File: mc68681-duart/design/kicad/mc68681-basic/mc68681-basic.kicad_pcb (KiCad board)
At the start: 4 copper layers, 80 x 110 mm, 35 parts, among them IC1 68681, IC2 74HCT245, IC3 74HCT245, IC4 74HCT245, IC5 74125, IC6 IC6_DECO.PLD, IC7 IC7_UART_.PLD, J1 Conn_02x32_Odd_Even, J2 EXTBUS, J3 UART_A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

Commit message: Initial work on schematic, board ripped up
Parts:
- removed JP1, JP2, JP3, JP4: Jumper, Connector_PinHeader_2.54mm:PinHeader_1x02_P2.54mm_Vertical
- added JP1-5: Conn_02x05_Odd_Even, Connector_PinHeader_2.54mm:PinHeader_2x05_P2.54mm_Vertical, F.Cu at (62.8, 136.7)
- IC1: value 68681 -> XR68C681CJTR-F; footprint Package_DIP:DIP-40_W15.24mm_Socket_LongPads -> Package_LCC:PLCC-44_THT-Socket
- moved C12 47.4 mm to (94.5, 75.4)
- moved C10 47.0 mm to (84.7, 75.4)
- moved C6 46.8 mm to (74.9, 75.3)
- moved C5 30.8 mm to (95.2, 114.3)
- moved C3 23.5 mm to (74.2, 114.3)
- moved Q1 22.4 mm to (82.3, 114.3), turned to 0 degrees
- moved IC1 22.1 mm to (86.0, 87.2)
- moved R2 14.1 mm to (79.6, 122.1), turned to 0 degrees
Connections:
- IC1 pad 1: A1 -> Net-(IC1-Pad1)
- IC1 pad 10: RXDB -> UDTACK
- IC1 pad 11: TXDB -> RXDB
- IC1 pad 12: CTSB -> Net-(IC1-Pad12)
- IC1 pad 13: OP3 -> TXDB
- IC1 pad 14: OP5 -> CTSB
- IC1 pad 15: OP7 -> OP3
- IC1 pad 16: BD1 -> OP5
- IC1 pad 17: BD3 -> OP7
- IC1 pad 18: BD5 -> BD1
- IC1 pad 19: BD7 -> BD3
- IC1 pad 2: IP3 -> A1
- IC1 pad 20: GND -> BD5
- IC1 pad 21: IRQ -> BD7
- IC1 pad 22: BD6 -> GND
- IC1 pad 23: BD4 -> Net-(IC1-Pad23)
- IC1 pad 24: BD2 -> IRQ
- IC1 pad 25: BD0 -> BD6
- IC1 pad 26: OP6 -> BD4
- IC1 pad 27: OP4 -> BD2
- IC1 pad 28: OP2 -> BD0
- IC1 pad 29: CTSA -> OP6
- IC1 pad 3: A2 -> IP3
- IC1 pad 30: TXDA -> OP4
- IC1 pad 31: RXDA -> OP2
- IC1 pad 32: Net-(C3-Pad1) -> CTSA
- IC1 pad 33: Net-(C5-Pad1) -> TXDA
- IC1 pad 34: RESET -> Net-(IC1-Pad34)
- IC1 pad 35: SEL -> RXDA
- IC1 pad 36: IP2 -> Net-(C3-Pad1)
- IC1 pad 37: Net-(IC1-Pad37) -> Net-(C5-Pad1)
- IC1 pad 38: IP5 -> RESET
- IC1 pad 39: IP4 -> SEL
- IC1 pad 4: IP1 -> A2
- IC1 pad 40: VCC -> IP2
- IC1 pad 5: A3 -> IP1
- IC1 pad 6: A4 -> A3
- IC1 pad 7: IP0 -> A4
- IC1 pad 8: RnW -> IP0
- IC1 pad 9: UDTACK -> RnW
- IC7 pad 14: VPA -> UVPA
- IC7 pad 15: Net-(IC7-Pad15) -> IACK
- IC7 pad 7: Net-(IC7-Pad7) -> A1
- IC7 pad 8: Net-(IC7-Pad8) -> A2
- IC7 pad 9: Net-(IC7-Pad9) -> A3
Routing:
- net IRQ: track 116.1 -> 44.0 mm, vias 1 -> 0
- net IP0: track 73.7 -> 9.14 mm, vias 1 -> 0
- net UDTACK: track 52.0 -> 0.00 mm
- net A3: track 109.1 -> 59.6 mm, vias 2 -> 1
- net IP1: track 81.8 -> 33.1 mm, vias 1 -> 0
- net A4: track 104.4 -> 55.9 mm, vias 2 -> 1
- net BD7: track 46.6 -> 4.86 mm, vias 2 -> 0
- net RnW: track 82.5 -> 41.1 mm, vias 3 -> 1
- net CTSA: track 40.0 -> 0.00 mm, vias 2 -> 0
- net BD1: track 38.9 -> 6.37 mm, vias 1 -> 0
- net BD6: track 38.3 -> 5.91 mm, vias 1 -> 0
- net BD3: track 32.9 -> 2.78 mm
- net IP3: track 88.5 -> 58.9 mm
- net A1: track 67.1 -> 38.6 mm, vias 2 -> 1
- net RXDA: track 190.3 -> 162.7 mm
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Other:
- board text added: "Copyright ©2021 Ross Bamford & Contributors"
- board text added: "Revision 2 - March 2021"
- board text added: "r1 Mainboard"
- board text added: "r1.2 Mainboard"
- board text removed: "Copyright ©2020 Ross Bamford & Contributors"
- board text removed: "DTACK Enable"
- board text removed: "MC68681"
- board text removed: "Revision 1.1 - August 2020"

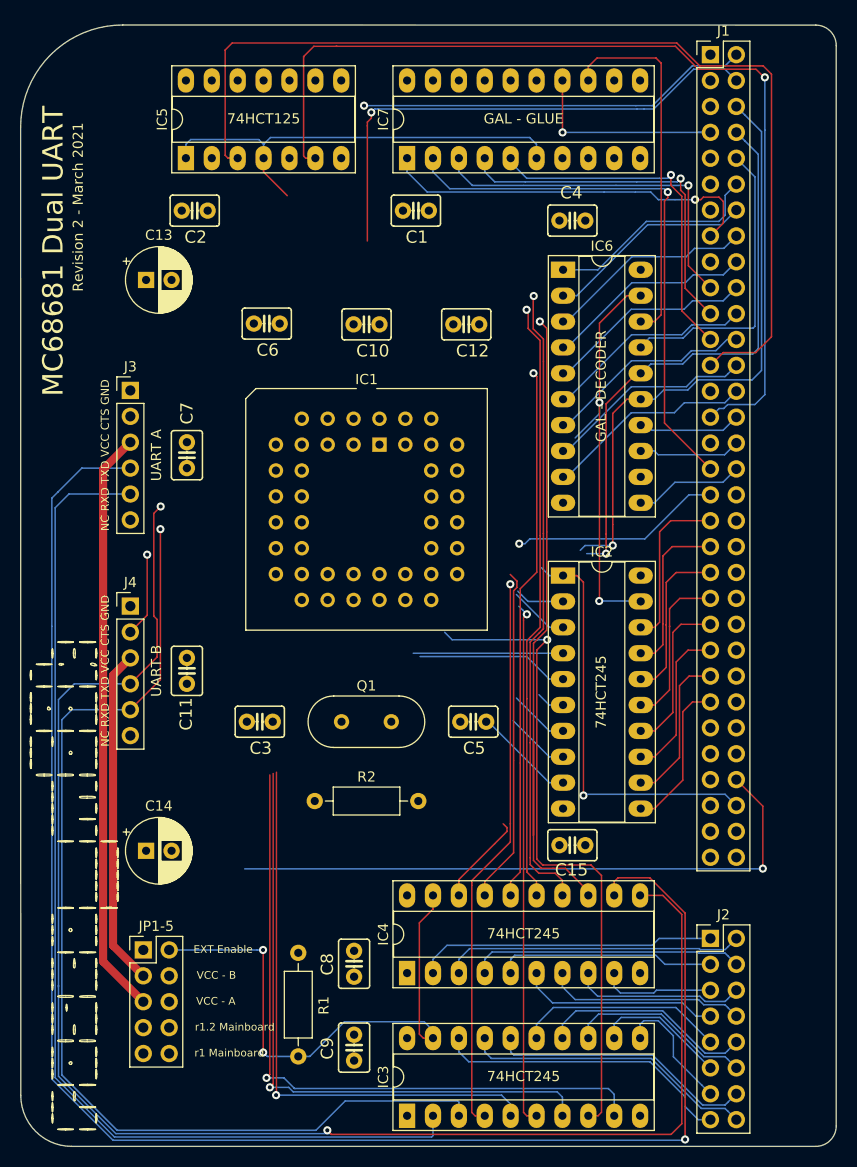
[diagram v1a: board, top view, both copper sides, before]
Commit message: First cut redo 68681 layout, add lib and pretty
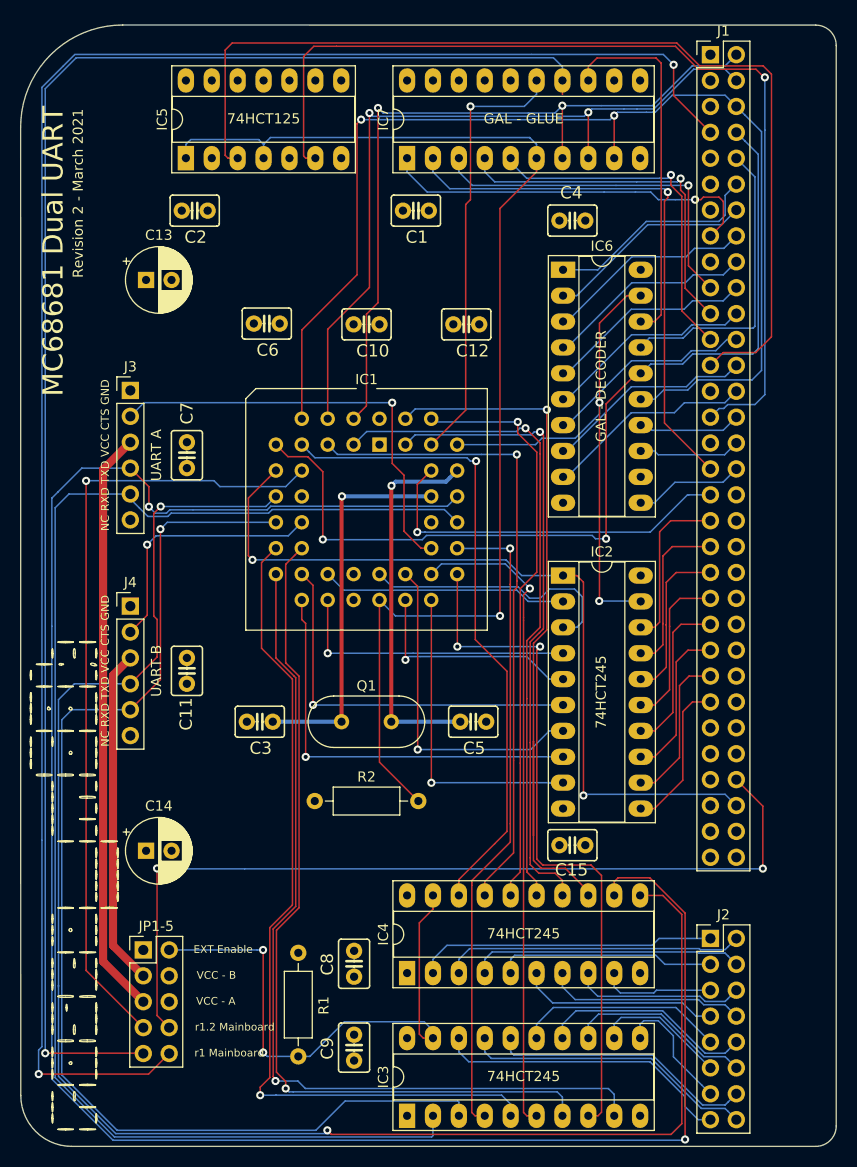
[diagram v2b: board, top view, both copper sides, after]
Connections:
- C3 pad 1: Net-(C3-Pad1) -> GND
- C3 pad 2: GND -> Net-(C3-Pad2)
- IC1 pad 36: Net-(C3-Pad1) -> Net-(C3-Pad2)
- Q1 pad 1: Net-(C3-Pad1) -> Net-(C3-Pad2)
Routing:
- net VPA: track 20.8 -> 182.4 mm, vias 1 -> 2
- net UVPA: track 0.00 -> 159.3 mm, vias 0 -> 1
- net UDTACK: track 0.00 -> 78.0 mm, vias 0 -> 1
- net IRQ: track 44.0 -> 119.6 mm, vias 0 -> 1
- net A3: track 59.6 -> 114.1 mm, vias 1 -> 2
- net IP0: track 9.14 -> 63.7 mm, vias 0 -> 1
- net IACK: track 0.00 -> 43.1 mm, vias 0 -> 1
- net CTSA: track 0.00 -> 42.7 mm, vias 0 -> 1
- net RnW: track 41.1 -> 79.9 mm, vias 1 -> 2
- net Net-(C3-Pad2): track 0.00 -> 37.6 mm, vias 0 -> 1
- net A4: track 55.9 -> 93.0 mm, vias 1 -> 2
- net Net-(C5-Pad1): track 0.00 -> 37.0 mm, vias 0 -> 1
- net A1: track 38.6 -> 75.3 mm, vias 1 -> 2
- net RXDA: track 162.7 -> 198.4 mm, vias 1 -> 2
- net BD3: track 2.78 -> 37.8 mm, vias 0 -> 1
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
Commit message: Fix 7pF footprint & prep for prototype fab
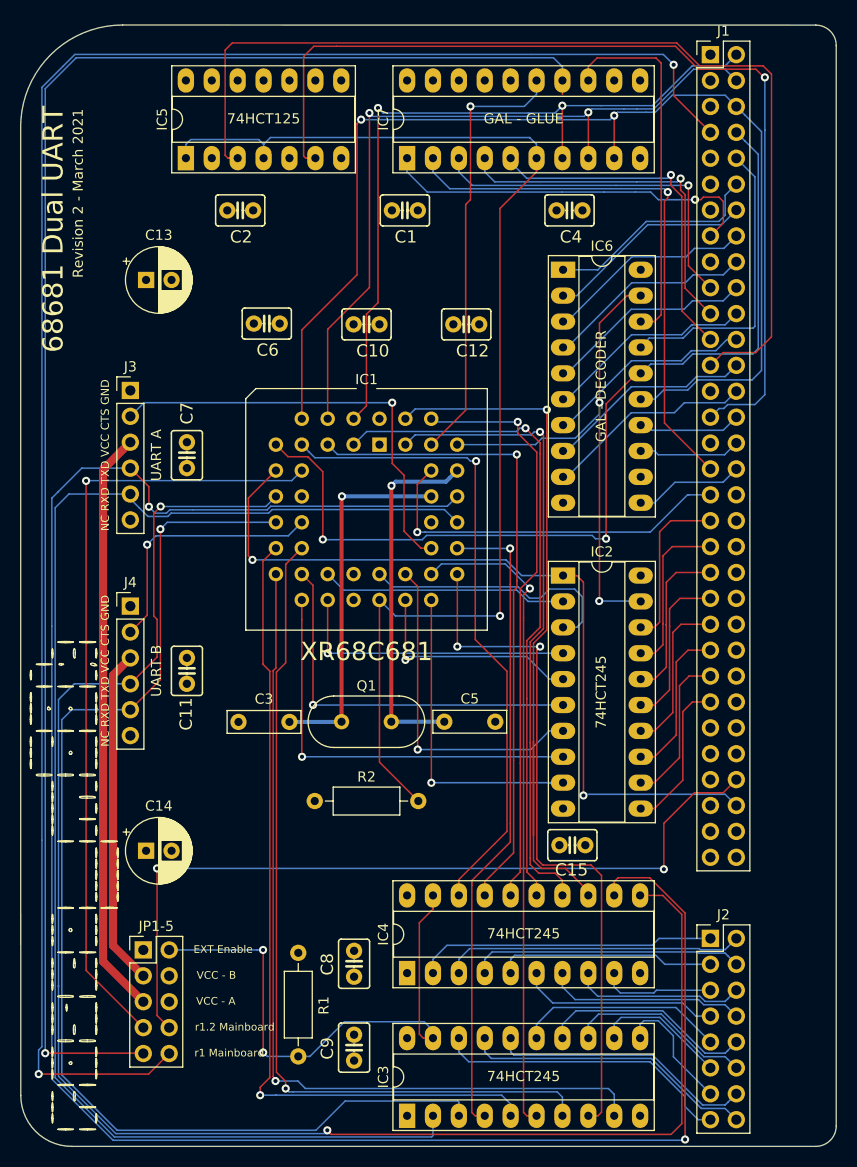
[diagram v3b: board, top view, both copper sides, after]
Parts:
- C3, C5: footprint rosco_m68k:C2.5-3 -> Capacitor_THT:C_Rect_L7.0mm_W2.0mm_P5.00mm
- moved C2 4.47 mm to (72.3, 64.2)
- moved C5 2.84 mm to (92.3, 114.3)
- moved C3 2.09 mm to (72.2, 114.4)
- moved C1 1.08 mm to (88.5, 64.2)
- moved C4 1.04 mm to (104.6, 64.2)
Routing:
- net DTACK: track 85.4 -> 79.3 mm
- net OP3: track 83.5 -> 81.5 mm
- net Net-(C3-Pad2): track 37.6 -> 36.0 mm
- net OP7: track 88.0 -> 86.4 mm
- net Net-(C5-Pad1): track 37.0 -> 35.4 mm
- net OP5: track 85.4 -> 84.3 mm
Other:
- board text added: "68681 Dual UART"
- board text added: "XR68C681"
- board text removed: "MC68681 Dual UART"
